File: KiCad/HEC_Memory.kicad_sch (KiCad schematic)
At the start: 10 parts, among them U13 74LS245, U14 74LS245, U15 74LS32, U16 74LS32, U2 AS6C4008-55PCN, U22 74LS02, U3 AS6C4008-55PCN, U4 CY7C199, U5 CY7C199, U9 74LS574

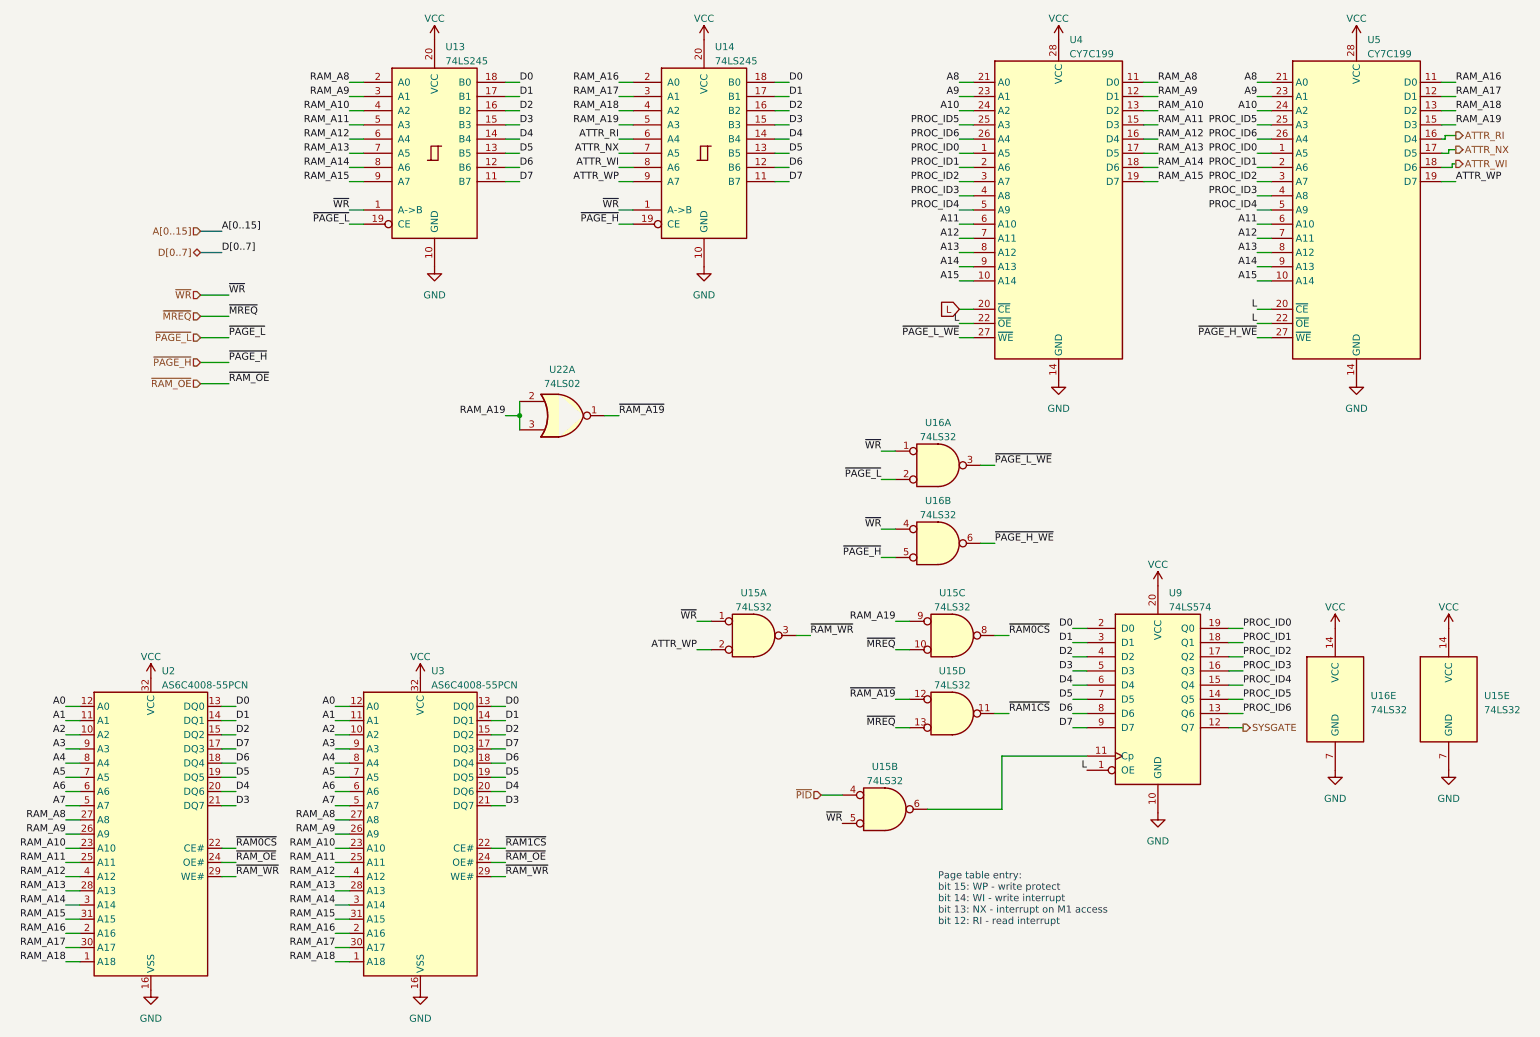
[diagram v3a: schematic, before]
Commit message: Add prototyping region
Add some prototyping regions to the board, since there WILL be bugs!
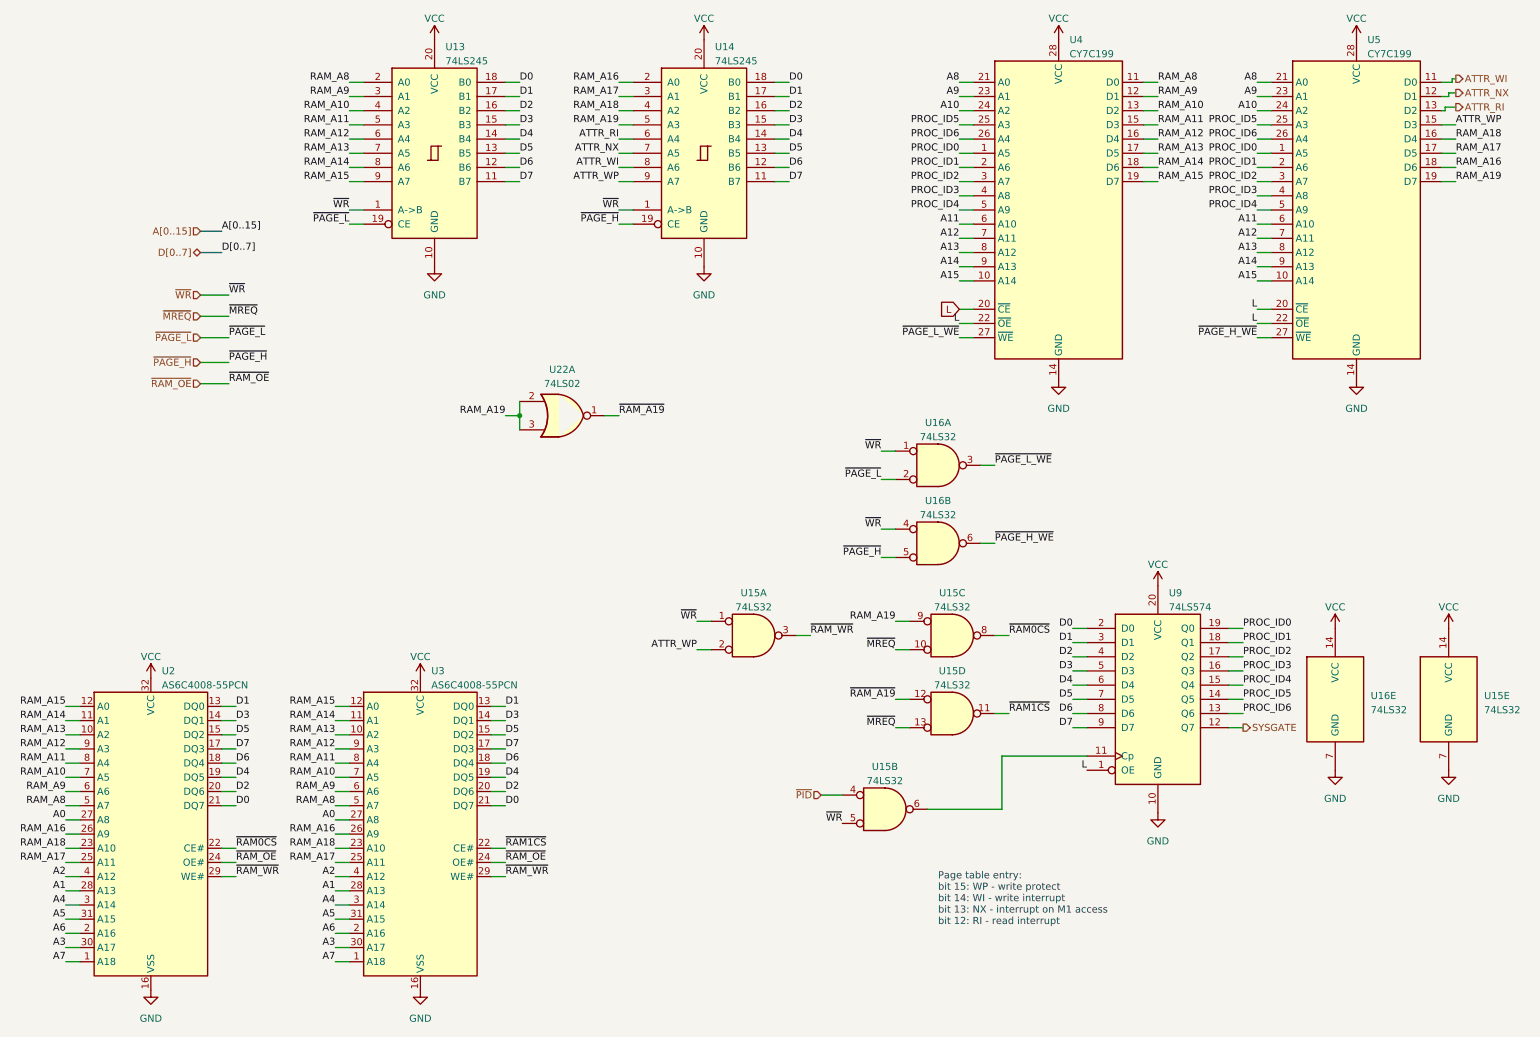
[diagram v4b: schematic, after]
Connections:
- net A0: now also U2.27 (A8), U3.27 (A8); no longer U2.12 (A0), U3.12 (A0)
- net A1: now also U2.28 (A13), U3.28 (A13); no longer U2.11 (A1), U3.11 (A1)
- net A2: now also U2.4 (A12), U3.4 (A12); no longer U2.10 (A2), U3.10 (A2)
- net A3: now also U2.30 (A17), U3.30 (A17); no longer U2.9 (A3), U3.9 (A3)
- net A4: now also U2.3 (A14), U3.3 (A14); no longer U2.8 (A4), U3.8 (A4)
- net A5: now also U2.31 (A15), U3.31 (A15); no longer U2.7 (A5), U3.7 (A5)
- net A6: now also U2.2 (A16), U3.2 (A16); no longer U2.6 (A6), U3.6 (A6)
- net A7: now also U2.1 (A18), U3.1 (A18); no longer U2.5 (A7), U3.5 (A7)
- net ATTR_NX: now also U5.12 (D1); no longer U5.17 (D5)
- net ATTR_RI: now also U5.13 (D2); no longer U5.16 (D4)
- net ATTR_WI: now also U5.11 (D0); no longer U5.18 (D6)
- net ATTR_WP: now also U5.15 (D3); no longer U5.19 (D7)
- net D0: now also U2.21 (DQ7), U3.21 (DQ7); no longer U2.13 (DQ0), U3.13 (DQ0)
- net D1: now also U2.13 (DQ0), U3.13 (DQ0); no longer U2.14 (DQ1), U3.14 (DQ1)
- net D2: now also U2.20 (DQ6), U3.20 (DQ6); no longer U2.15 (DQ2), U3.15 (DQ2)
- net D3: now also U2.14 (DQ1), U3.14 (DQ1); no longer U2.21 (DQ7), U3.21 (DQ7)
- net D4: now also U2.19 (DQ5), U3.19 (DQ5); no longer U2.20 (DQ6), U3.20 (DQ6)
- net D5: now also U2.15 (DQ2), U3.15 (DQ2); no longer U2.19 (DQ5), U3.19 (DQ5)
- net RAM_A10: now also U2.7 (A5), U3.7 (A5); no longer U2.23 (A10), U3.23 (A10)
- net RAM_A11: now also U2.8 (A4), U3.8 (A4); no longer U2.25 (A11), U3.25 (A11)
- net RAM_A12: now also U2.9 (A3), U3.9 (A3); no longer U2.4 (A12), U3.4 (A12)
- net RAM_A13: now also U2.10 (A2), U3.10 (A2); no longer U2.28 (A13), U3.28 (A13)
- net RAM_A14: now also U2.11 (A1), U3.11 (A1); no longer U2.3 (A14), U3.3 (A14)
- net RAM_A15: now also U2.12 (A0), U3.12 (A0); no longer U2.31 (A15), U3.31 (A15)
- net RAM_A16: now also U2.26 (A9), U3.26 (A9), U5.18 (D6); no longer U2.2 (A16), U3.2 (A16), U5.11 (D0)
- net RAM_A17: now also U2.25 (A11), U3.25 (A11), U5.17 (D5); no longer U2.30 (A17), U3.30 (A17), U5.12 (D1)
- net RAM_A18: now also U2.23 (A10), U3.23 (A10), U5.16 (D4); no longer U2.1 (A18), U3.1 (A18), U5.13 (D2)
- net RAM_A19: now also U5.19 (D7); no longer U5.15 (D3)
- net RAM_A8: now also U2.5 (A7), U3.5 (A7); no longer U2.27 (A8), U3.27 (A8)
- net RAM_A9: now also U2.6 (A6), U3.6 (A6); no longer U2.26 (A9), U3.26 (A9)

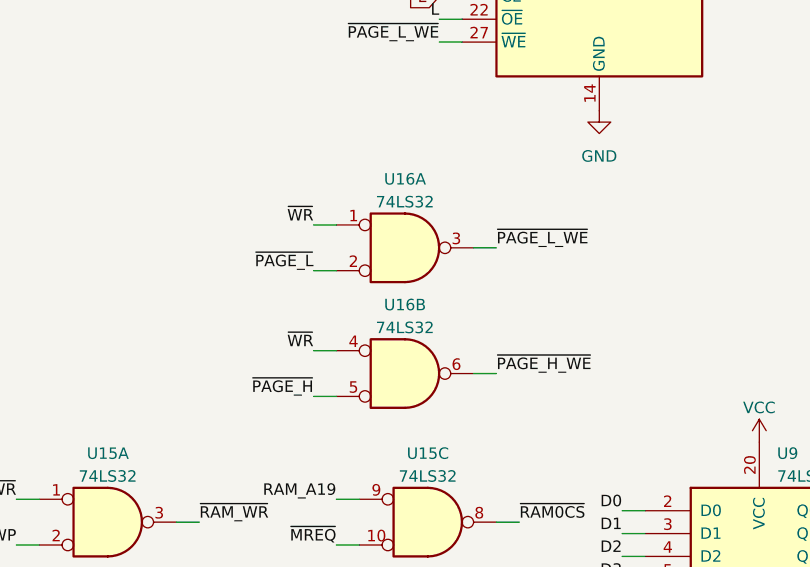
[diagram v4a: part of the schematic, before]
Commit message: More routing
Swapped U15 and U16, minor adjustments to schematic. routing of power lines.
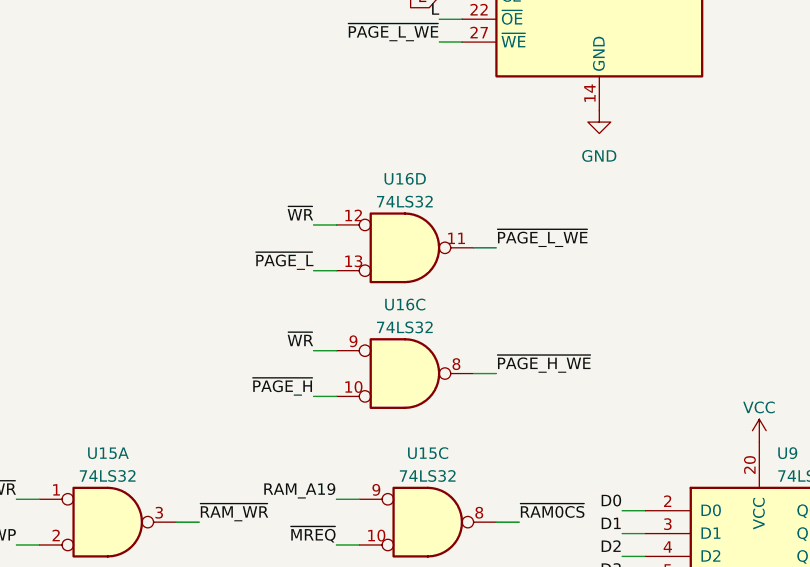
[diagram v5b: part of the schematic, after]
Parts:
- removed unit 1 of U16
- removed unit 2 of U16
- added unit 4 of U16
- added unit 3 of U16
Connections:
- net ~{PAGE_H_WE}: now also U16.8
- net ~{PAGE_H}: now also U16.10
- net ~{PAGE_L_WE}: now also U16.11
- net ~{PAGE_L}: now also U16.13
- net ~{WR}: now also U16.12, U16.9
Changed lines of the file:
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@@
+    )
+  )
+  (symbol (lib_id "74xx:74LS32") (at 179.07 96.52 0) (unit 4) (convert 2)
+    (in_bom yes) (on_board yes) (dnp no) (fields_autoplaced)
+    (property "Reference" "U16" (at 179.07 88.9 0)
+      (effects (font (size 1.27 1.27)))
+    )
+    (property "Value" "74LS32" (at 179.07 91.44 0)
+      (effects (font (size 1.27 1.27)))
+    )
+    (property "Footprint" "Package_DIP:DIP-14_W7.62mm_Socket" (at 179.07 96.52 0)
+      (effects (font (size 1.27 1.27)) hide)
+    )
+    (property "Datasheet" "http://www.ti.com/lit/gpn/sn74LS32" (at 179.07 96.52 0)
+      (effects (font (size 1.27 1.27)) hide)
+    )
+    (pin "1")
+    (pin "2")
+    (pin "3")
+    (pin "4")
+    (pin "5")
+    (pin "6")
+    (pin "10")
+    (pin "8")
+    (pin "9")
+    (pin "11")
+    (pin "12")
+    (pin "13")
+    (pin "14")
+    (pin "7")
+    (instances
+      (project "HEC1"
+        (path "/87935374-b60a-4f41-99da-94b76103dd77/933a6f90-eb98-4eb1-8c19-8a76228aece1"
+          (reference "U16") (unit 4)
+        )
+        (path "/87935374-b60a-4f41-99da-94b76103dd77/73a0c68b-1e42-4c0d-ae31-b1a96d0648bb"
+          (reference "U16") (unit 4)
+        )
+      )
     )
   )
@@
         (path "/87935374-b60a-4f41-99da-94b76103dd77/933a6f90-eb98-4eb1-8c19-8a76228aece1"
           (reference "#PWR016") (unit 1)
+        )
+      )
+    )
+  )
+  (symbol (lib_id "74xx:74LS32") (at 179.07 110.49 0) (unit 3) (convert 2)
+    (in_bom yes) (on_board yes) (dnp no) (fields_autoplaced)
+    (property "Reference" "U16" (at 179.07 102.87 0)
+      (effects (font (size 1.27 1.27)))
+    )
+    (property "Value" "74LS32" (at 179.07 105.41 0)
+      (effects (font (size 1.27 1.27)))
+    )
+    (property "Footprint" "Package_DIP:DIP-14_W7.62mm_Socket" (at 179.07 110.49 0)
+      (effects (font (size 1.27 1.27)) hide)
+    )
+    (property "Datasheet" "http://www.ti.com/lit/gpn/sn74LS32" (at 179.07 110.49 0)
+      (effects (font (size 1.27 1.27)) hide)
+    )
+    (pin "1")
+    (pin "2")
+    (pin "3")
+    (pin "4")
+    (pin "5")
+    (pin "6")
+    (pin "10")
+    (pin "8")
+    (pin "9")
+    (pin "11")
+    (pin "12")
+    (pin "13")
+    (pin "14")
+    (pin "7")
+    (instances
+      (project "HEC1"
+        (path "/87935374-b60a-4f41-99da-94b76103dd77/933a6f90-eb98-4eb1-8c19-8a76228aece1"
+          (reference "U16") (unit 3)
+        )
+        (path "/87935374-b60a-4f41-99da-94b76103dd77/73a0c68b-1e42-4c0d-ae31-b1a96d0648bb"
+          (reference "U16") (unit 3)
         )
       )
@@
     )
   )
-  (symbol (lib_id "74xx:74LS32") (at 179.07 96.52 0) (unit 1) (convert 2)
-    (in_bom yes) (on_board yes) (dnp no) (fields_autoplaced)
-    (property "Reference" "U16" (at 179.07 88.9 0)
-      (effects (font (size 1.27 1.27)))
-    )
-    (property "Value" "74LS32" (at 179.07 91.44 0)
-      (effects (font (size 1.27 1.27)))
-    )
-    (property "Footprint" "Package_DIP:DIP-14_W7.62mm_Socket" (at 179.07 96.52 0)
-      (effects (font (size 1.27 1.27)) hide)
-    )
-    (property "Datasheet" "http://www.ti.com/lit/gpn/sn74LS32" (at 179.07 96.52 0)
-      (effects (font (size 1.27 1.27)) hide)
-    )
-    (pin "1")
-    (pin "2")
-    (pin "3")
-    (pin "4")
-    (pin "5")
-    (pin "6")
-    (pin "10")
-    (pin "8")
-    (pin "9")
-    (pin "11")
-    (pin "12")
-    (pin "13")
-    (pin "14")
-    (pin "7")
-    (instances
-      (project "HEC1"
-        (path "/87935374-b60a-4f41-99da-94b76103dd77/933a6f90-eb98-4eb1-8c19-8a76228aece1"
-          (reference "U16") (unit 1)
-        )
-      )
-    )
-  )
   (symbol (lib_id "power:GND") (at 200.66 81.28 0) (unit 1)
     (in_bom yes) (on_board yes) (dnp no) (fields_autoplaced)
@@
         )
       )
-    )
-  )
-  (symbol (lib_id "74xx:74LS32") (at 179.07 110.49 0) (unit 2) (convert 2)
-    (in_bom yes) (on_board yes) (dnp no) (fields_autoplaced)
-    (property "Reference" "U16" (at 179.07 102.87 0)
-      (effects (font (size 1.27 1.27)))
-    )
-    (property "Value" "74LS32" (at 179.07 105.41 0)
-      (effects (font (size 1.27 1.27)))
-    )
-    (property "Footprint" "Package_DIP:DIP-14_W7.62mm_Socket" (at 179.07 110.49 0)
-      (effects (font (size 1.27 1.27)) hide)
-    )
-    (property "Datasheet" "http://www.ti.com/lit/gpn/sn74LS32" (at 179.07 110.49 0)
-      (effects (font (size 1.27 1.27)) hide)
-    )
-    (pin "1")
-    (pin "2")
-    (pin "3")
-    (pin "4")
-    (pin "5")
-    (pin "6")
-    (pin "10")
-    (pin "8")
-    (pin "9")
-    (pin "11")
-    (pin "12")
-    (pin "13")
-    (pin "14")
-    (pin "7")
-    (instances
-      (project "HEC1"
-        (path "/87935374-b60a-4f41-99da-94b76103dd77/933a6f90-eb98-4eb1-8c19-8a76228aece1"
-          (reference "U16") (unit 2)
-        )
-      )

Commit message: Bug fixes
fixed some bugs introduced to the schematic. More routing.
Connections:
- net D0: now also U9.6 (D4); no longer U9.2 (D0)
- net D1: now also U9.7 (D5); no longer U9.3 (D1)
- net D2: now also U9.9 (D7); no longer U9.4 (D2)
- net D3: now also U9.8 (D6); no longer U9.5 (D3)
- net D4: now also U9.5 (D3); no longer U9.6 (D4)
- net D5: now also U9.4 (D2); no longer U9.7 (D5)
- net D6: now also U9.3 (D1); no longer U9.8 (D6)
- net D7: now also U9.2 (D0); no longer U9.9 (D7)
- net PROC_ID0: now also U9.15 (Q4); no longer U9.19 (Q0)
- net PROC_ID1: now also U9.14 (Q5); no longer U9.18 (Q1)
- net PROC_ID2: now also U9.12 (Q7); no longer U9.17 (Q2)
- net PROC_ID3: now also U9.13 (Q6); no longer U9.16 (Q3)
- net PROC_ID4: now also U9.16 (Q3); no longer U9.15 (Q4)
- net PROC_ID5: now also U9.17 (Q2); no longer U9.14 (Q5)
- net PROC_ID6: now also U9.18 (Q1); no longer U9.13 (Q6)
- net SYSGATE: now also U9.19 (Q0); no longer U9.12 (Q7)
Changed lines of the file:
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@@
-    (stroke (width 0) (type default))
-  )
-  (wire (pts (xy 233.68 125.73) (xy 231.14 125.73))
     (stroke (width 0) (type default))
   )
@@
     (stroke (width 0) (type default))
   )
+  (wire (pts (xy 232.41 125.73) (xy 231.14 125.73))
+    (stroke (width 0) (type default))
+  )
   (wire (pts (xy 124.46 45.72) (xy 121.92 45.72))
     (stroke (width 0) (type default))
@@
     (stroke (width 0) (type default))
   )
+  (wire (pts (xy 233.045 125.095) (xy 232.41 125.095))
+    (stroke (width 0) (type default))
+  )
   (wire (pts (xy 71.12 167.64) (xy 73.66 167.64))
     (stroke (width 0) (type default))
@@
   )
   (wire (pts (xy 149.86 27.94) (xy 152.4 27.94))
+    (stroke (width 0) (type default))
+  )
+  (wire (pts (xy 232.41 125.095) (xy 232.41 125.73))
     (stroke (width 0) (type default))
   )
@@
     (effects (font (size 1.27 1.27)) (justify left bottom))
   )
-  (label "D4" (at 203.2 135.89 180) (fields_autoplaced)
+  (label "D4" (at 203.2 133.35 180) (fields_autoplaced)
     (effects (font (size 1.27 1.27)) (justify right bottom))
   )
@@
     (effects (font (size 1.27 1.27)) (justify right bottom))
   )
-  (label "D2" (at 203.2 130.81 180) (fields_autoplaced)
+  (label "D2" (at 203.2 143.51 180) (fields_autoplaced)
     (effects (font (size 1.27 1.27)) (justify right bottom))
   )
@@
     (effects (font (size 1.27 1.27)) (justify right bottom))
   )
-  (label "D6" (at 203.2 140.97 180) (fields_autoplaced)
-    (effects (font (size 1.27 1.27)) (justify right bottom))
-  )
-  (label "D1" (at 203.2 128.27 180) (fields_autoplaced)
+  (label "D6" (at 203.2 128.27 180) (fields_autoplaced)
+    (effects (font (size 1.27 1.27)) (justify right bottom))
+  )
+  (label "D1" (at 203.2 138.43 180) (fields_autoplaced)
     (effects (font (size 1.27 1.27)) (justify right bottom))
   )
@@
     (effects (font (size 1.27 1.27)) (justify right bottom))
   )
-  (label "PROC_ID1" (at 233.68 128.27 0) (fields_autoplaced)
+  (label "PROC_ID1" (at 233.68 138.43 0) (fields_autoplaced)
     (effects (font (size 1.27 1.27)) (justify left bottom))
   )
@@
     (effects (font (size 1.27 1.27)) (justify left bottom))
   )
-  (label "PROC_ID4" (at 233.68 135.89 0) (fields_autoplaced)
+  (label "PROC_ID4" (at 233.68 133.35 0) (fields_autoplaced)
     (effects (font (size 1.27 1.27)) (justify left bottom))
   )
@@
     (effects (font (size 1.27 1.27)) (justify left bottom))
   )
-  (label "PROC_ID5" (at 233.68 138.43 0) (fields_autoplaced)
+  (label "PROC_ID5" (at 233.68 130.81 0) (fields_autoplaced)
     (effects (font (size 1.27 1.27)) (justify left bottom))
   )
@@
     (effects (font (size 1.27 1.27)) (justify right bottom))
   )
-  (label "PROC_ID3" (at 233.68 133.35 0) (fields_autoplaced)
+  (label "PROC_ID3" (at 233.68 140.97 0) (fields_autoplaced)
     (effects (font (size 1.27 1.27)) (justify left bottom))
   )
@@
     (effects (font (size 1.27 1.27)) (justify left bottom))
   )
-  (label "PROC_ID6" (at 233.68 140.97 0) (fields_autoplaced)
+  (label "PROC_ID6" (at 233.68 128.27 0) (fields_autoplaced)
     (effects (font (size 1.27 1.27)) (justify left bottom))
   )
@@
     (effects (font (size 1.27 1.27)) (justify left bottom))
   )
-  (label "D0" (at 203.2 125.73 180) (fields_autoplaced)
-    (effects (font (size 1.27 1.27)) (justify right bottom))
-  )
-  (label "D7" (at 203.2 143.51 180) (fields_autoplaced)
+  (label "D0" (at 203.2 135.89 180) (fields_autoplaced)
+    (effects (font (size 1.27 1.27)) (justify right bottom))
+  )
+  (label "D7" (at 203.2 125.73 180) (fields_autoplaced)
     (effects (font (size 1.27 1.27)) (justify right bottom))
   )
@@
     (effects (font (size 1.27 1.27)) (justify right bottom))
   )
-  (label "PROC_ID0" (at 233.68 125.73 0) (fields_autoplaced)
+  (label "PROC_ID0" (at 233.68 135.89 0) (fields_autoplaced)
     (effects (font (size 1.27 1.27)) (justify left bottom))
   )
@@
     (effects (font (size 1.27 1.27)) (justify right bottom))
   )
-  (label "PROC_ID2" (at 233.68 130.81 0) (fields_autoplaced)
+  (label "PROC_ID2" (at 233.68 143.51 0) (fields_autoplaced)
     (effects (font (size 1.27 1.27)) (justify left bottom))
   )
@@
     (effects (font (size 1.27 1.27)) (justify right bottom))
   )
-  (label "D3" (at 203.2 133.35 180) (fields_autoplaced)
+  (label "D3" (at 203.2 140.97 180) (fields_autoplaced)
     (effects (font (size 1.27 1.27)) (justify right bottom))
   )
@@
     (effects (font (size 1.27 1.27)) (justify left bottom))
   )
-  (label "D5" (at 203.2 138.43 180) (fields_autoplaced)
+  (label "D5" (at 203.2 130.81 180) (fields_autoplaced)
     (effects (font (size 1.27 1.27)) (justify right bottom))
   )
@@
     (effects (font (size 1.27 1.27)) (justify right))
   )
-  (hierarchical_label "SYSGATE" (shape output) (at 233.68 143.51 0) (fields_autoplaced)
+  (hierarchical_label "SYSGATE" (shape output) (at 233.045 125.095 0) (fields_autoplaced)
     (effects (font (size 1.27 1.27)) (justify left))
   )
